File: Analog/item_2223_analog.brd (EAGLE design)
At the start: 100 x 40 mm, 74 parts, among them IC1 MCP1525TO, IC2 MCP6004SO, IC4 MCP6004SO, IC5 MCP6004SO, IC6 MCP3204SL, IC7 LM336LP

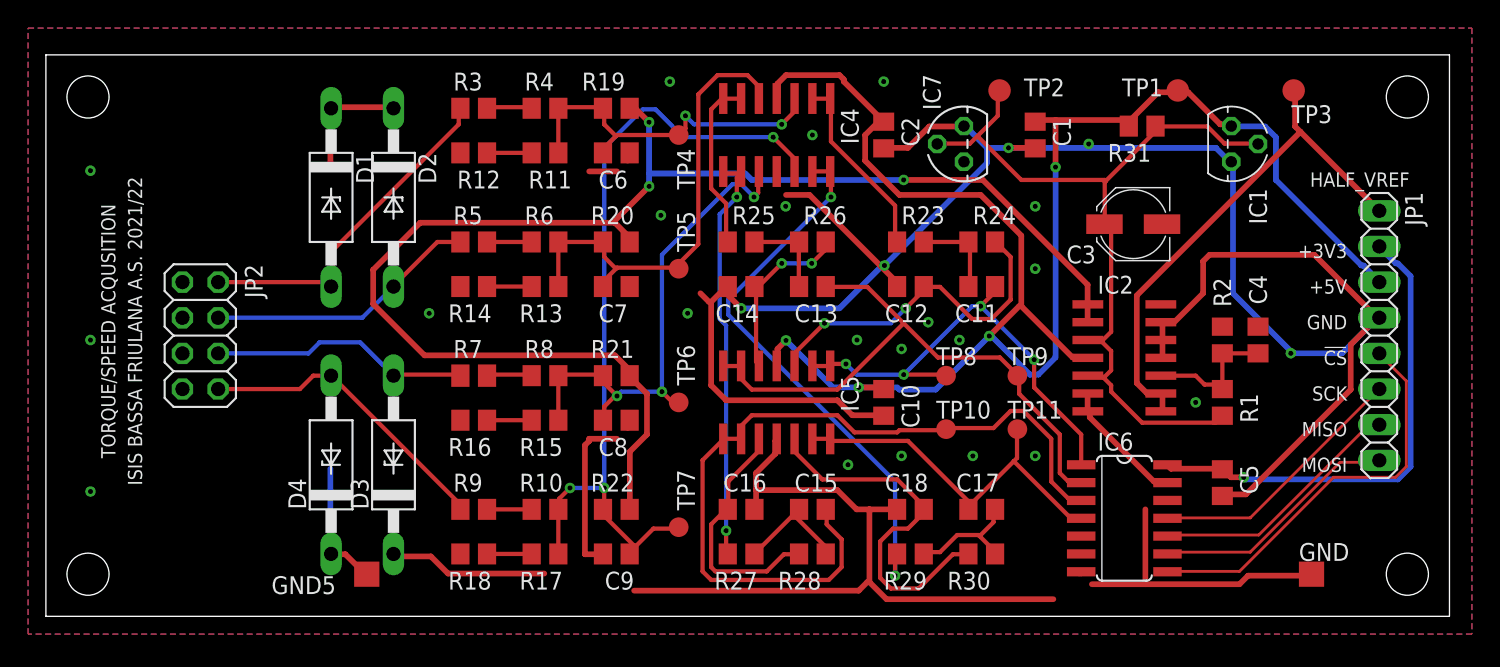
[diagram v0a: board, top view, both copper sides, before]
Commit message: ingresso differenziale e AGND
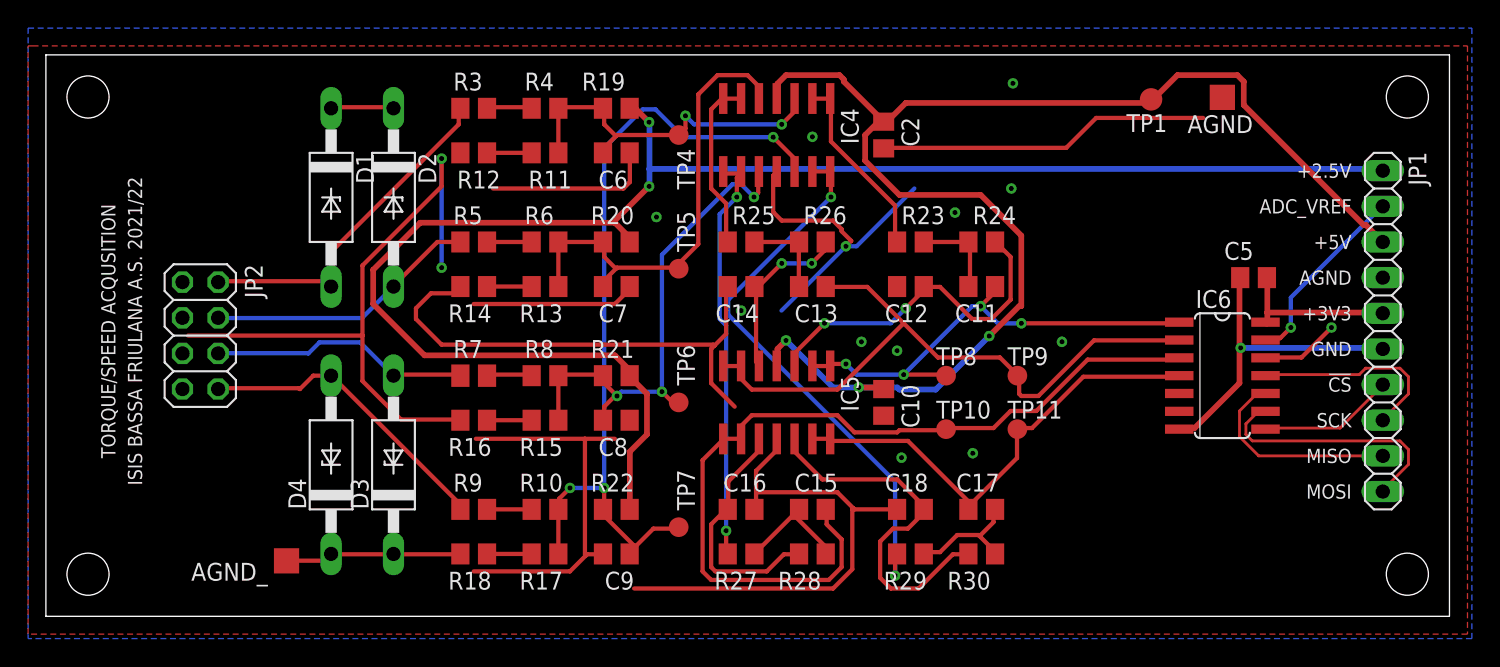
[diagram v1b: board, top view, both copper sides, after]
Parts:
- removed C1, C4: 100nF, rcl_LargePads:C0805
- removed C3: 10uF / 16V, rcl_LargePads:PANASONIC_C
- removed GND, GND5: TPTP18SQ, testpad:TP18SQ
- removed IC1: MCP1525TO, MCP1525_MCP1541:TO92
- removed IC2: MCP6004SO, MCP6002_MCP6004:SO14
- removed IC7: LM336LP, linear:TO92
- removed R1, R2: 6.8k, rcl_LargePads:R0805
- removed R31: 2.7k, rcl:R0805
- removed TP2, TP3: TPTP16R, testpad:TP16R
- added AGND, AGND_: TPTP18SQ, testpad:TP18SQ
- JP1: device pinhead:1X08 -> pinhead:1X10
- moved C5 14.8 mm to (86.0, 24.1), turned to 180 degrees
- moved IC6 12.3 mm to (83.8, 17.1)
- moved TP1 2.01 mm to (78.7, 36.8)
- moved JP1 0.41 mm to (95.2, 20.3)
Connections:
- removed net ADC_HALF_VREF: IC2.8, IC2.9, JP1.1, TP3.TP
- removed net N$3: C4.1, IC2.10, R1.1, R2.2
- removed net VREF: C3.+, IC1.2, IC2.3, IC2.5, IC7.2, R1.2, R31.1, TP2.TP
- new net AGND: AGND.TP, AGND_.TP, C10.2, C12.2, C14.2, C16.2, C18.2, C2.2, C6.2, C7.2, C8.2, C9.2, D1.C, D2.C, D3.C, D4.C, IC4.11, IC5.11, IC6.12, JP1.4, JP2.1, JP2.3, JP2.5, JP2.7, R12.2, R14.2, R16.2, R18.2
- net !CS_MCP3204!: now also JP1.7; no longer JP1.5
- net +2.5V: now also JP1.1; no longer IC2.1, IC2.2
- net +3V3: now also JP1.5; no longer JP1.2
- net +5V: no longer C1.1, IC1.3, IC2.4, R31.2
- net ADC_VREF: now also JP1.2; no longer IC2.6, IC2.7
- net GND: now also JP1.6; no longer C1.2, C10.2, C12.2, C14.2, C16.2, C18.2, C2.2, C3.-, C4.2, C6.2, C7.2, C8.2, C9.2, D1.C, D2.C, D3.C, D4.C, GND.TP, GND5.TP, IC1.1, IC2.11, IC2.12, IC2.13, IC4.11, IC5.11, IC6.12, IC7.3, JP1.4, JP2.1, JP2.3, JP2.5, JP2.7, R12.2, R14.2, R16.2, R18.2, R2.1
- net VSPI_MISO: now also JP1.9; no longer JP1.7
- net VSPI_MOSI: now also JP1.10; no longer JP1.8
- net VSPI_SCK: now also JP1.8; no longer JP1.6
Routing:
- net GND: track 271.2 -> 23.6 mm, vias 26 -> 1
- net AGND: track 0.00 -> 246.3 mm, vias 0 -> 15
- net VREF: track 59.1 -> 0.00 mm
- net ADC_HALF_VREF: track 37.3 -> 0.00 mm
- net +3V3: track 34.8 -> 11.7 mm, vias 1 -> 0
- net +5V: track 120.2 -> 100.3 mm, vias 4 -> 3
- net !CS_MCP3204!: track 29.0 -> 9.69 mm
- net +2.5V: track 101.3 -> 116.5 mm, vias 3 -> 2
- net N$3: track 9.87 -> 0.00 mm
- net A_SPEED2: track 27.3 -> 34.0 mm
- net A_TORQUE2: track 42.4 -> 46.9 mm
- net VSPI_SCK: track 18.9 -> 14.5 mm
- net ADC_VREF: track 9.24 -> 13.6 mm, vias 0 -> 1
- net A_SPEED1: track 57.6 -> 61.8 mm
- net VSPI_MISO: track 18.4 -> 15.0 mm
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- added copper zone on layer 1, net AGND
- added copper zone on layer 16, net AGND
- removed copper zone on layer 1, net GND
- removed copper zone on layer 16, net GND
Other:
- board text added: "+2.5V"
- board text added: "ADC_VREF"
- board text added: "AGND"
- board text removed: "HALF_VREF"
